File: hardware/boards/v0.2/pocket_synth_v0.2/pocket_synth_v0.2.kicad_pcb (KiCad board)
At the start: 6 copper layers, 155 x 162 mm, 60 parts, among them J1 Conn_ARM_JTAG_SWD_10, J10 Conn_01x05_Pin, J11 Conn_01x02_Pin, J12 Conn_01x03_Pin, J13 INPUT, J14 UART4, J2 USB, J3 AudioJack3, J4 AudioJack3, J5 AudioJack3, J6 AudioJack3, J7 DISPLAY, J8 Micro_SD_Card_Det2, J9 USART4, SW1 SW_Push, SW2 SW_Push, SW3 SW_Push, SW4 SW_Push, U1 STM32H743XIHx, U3 SDRAM, U4 STM32H753VIHx, U5 W25Q128JVS, Y1 32.768kHz, Y2 HSE

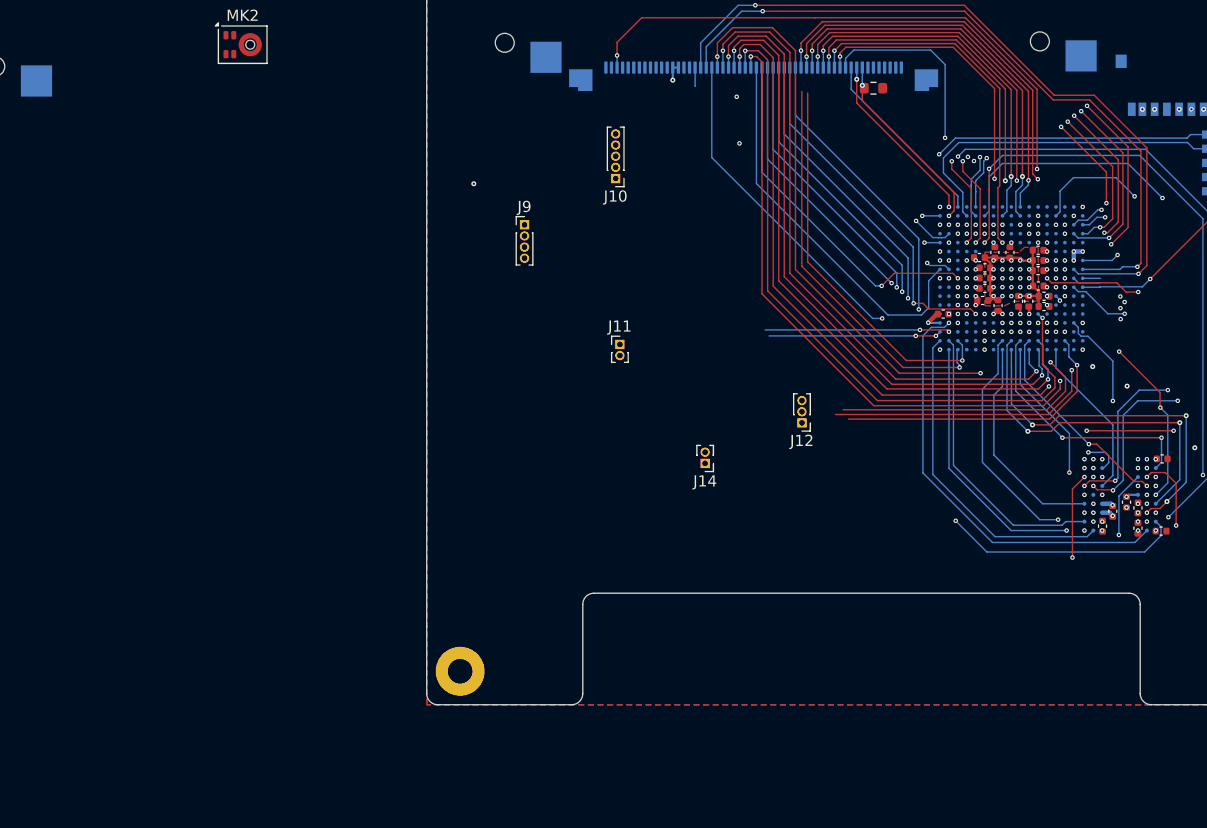
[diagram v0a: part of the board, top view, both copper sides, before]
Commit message: add NINA-W13 Wifi module and BM83 Bluetooth Audio
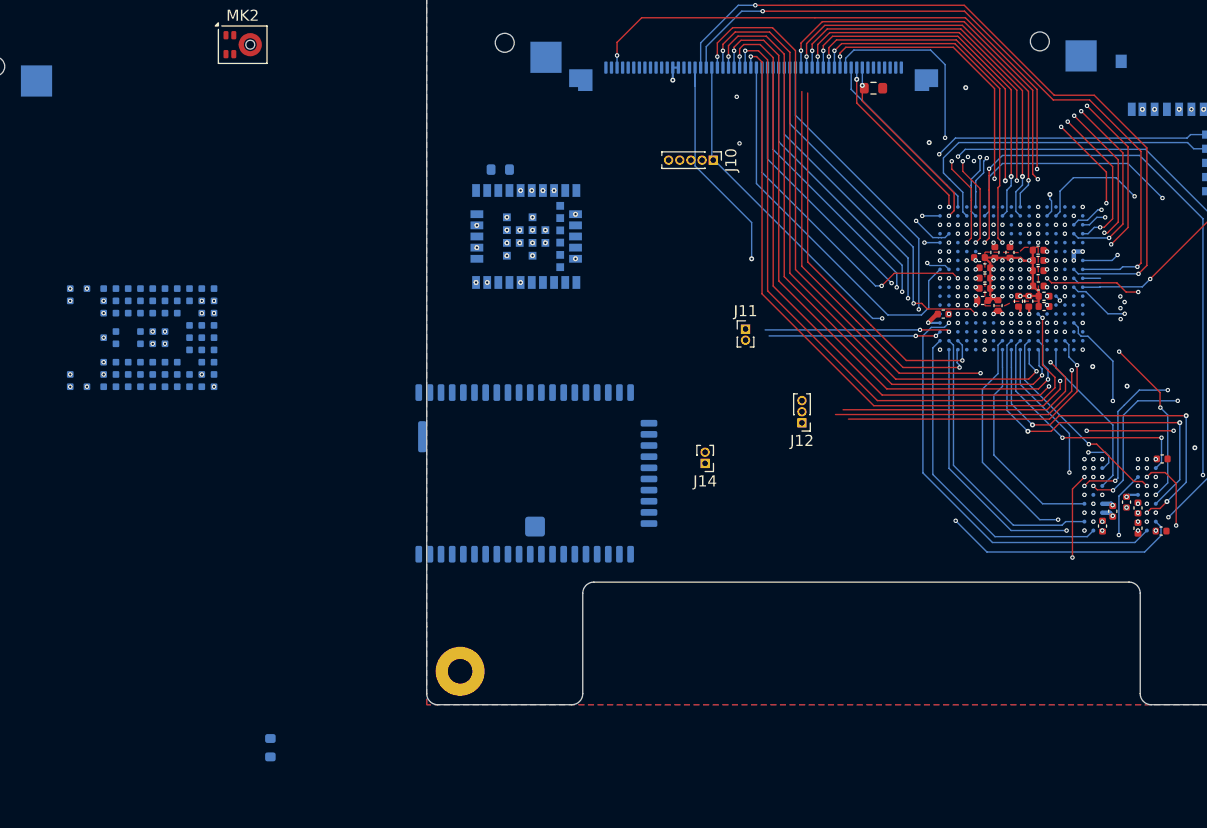
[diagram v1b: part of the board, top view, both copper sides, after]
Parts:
- removed J9: USART4, Connector_PinHeader_1.00mm:PinHeader_1x04_P1.00mm_Vertical
- added R4: R, Resistor_SMD:R_0603_1608Metric, B.Cu at (-2.02, 85.9)
- added R5: R, Resistor_SMD:R_0603_1608Metric, B.Cu at (18.6, 34.0)
- added U2: NORA-W40, Northernpaws_RF:NORA-W40, B.Cu at (-12.6, 49.1)
- added U6: Microchip_BM83, RF_Module:Microchip_BM83, B.Cu at (16.2, 61.2)
- added U7: NINA-W13, Northernpaws_RF:ublox-NINA-W13, B.Cu at (20.9, 40.0)
- J8: value Micro_SD_Card_Det2 -> SDCARD
- moved J11 11.4 mm to (40.6, 48.3)
- moved J10 8.90 mm to (37.7, 33.1), turned to -90 degrees
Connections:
- J8 pad 6: unconnected-(J8-VSS-Pad6) -> GND
- U1 pad D14: Net-(J9-Pin_2) -> /USART1_RX
- U1 pad D15: Net-(J9-Pin_1) -> /USART1_TX
- U1 pad E16: Net-(J9-Pin_4) -> /USART1_RTS
- U1 pad E17: Net-(J9-Pin_3) -> /USART1_CTS
- U1 pad F16: unconnected-(U1-PG7-PadF16) -> /LCD_CLK
- U1 pad H3: /LCD_CLK -> unconnected-(U1-PI14-PadH3)
- U5 pad 8: unconnected-(U5-VCC-Pad8) -> +3.3V
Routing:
- net /USART1_TX: track 0.00 -> 38.0 mm, vias 0 -> 2
- net Net-(J9-Pin_2): track 34.5 -> 0.00 mm, vias 1 -> 0
- net /LCD_CLK: track 4.82 -> 39.2 mm, vias 1 -> 2
- net /USART1_RX: track 0.00 -> 34.3 mm, vias 0 -> 2
- net Net-(J9-Pin_1): track 33.2 -> 0.00 mm, vias 1 -> 0
- net Net-(J9-Pin_4): track 33.2 -> 0.00 mm, vias 1 -> 0
- net Net-(J9-Pin_3): track 33.1 -> 0.00 mm, vias 1 -> 0
- net /USART1_RTS: track 0.00 -> 32.6 mm, vias 0 -> 2
- net /USART1_CTS: track 0.00 -> 31.3 mm, vias 0 -> 2
- net /QSPI1_CS: track 0.00 -> 2.15 mm, vias 0 -> 1
- net GND: vias 65 -> 102
- net +3.3V: vias 36 -> 41
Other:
- outline, holes or cut-outs redrawn
- board text removed: "BLUETOOTH MODULE FSC-BT1035"
- board text removed: "WIFI NORA-W40"
